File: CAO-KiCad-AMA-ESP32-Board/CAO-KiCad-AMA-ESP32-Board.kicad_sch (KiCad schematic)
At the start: 85 parts, among them J13 DHT Sensor, J14 Pot, J15 Select A, J16 Select B, J17 I2C, J3 Conn_01x19, J4 Conn_01x19, J5 Micro_SD_Card, J6 Servo, J7 I2C, J8 5V Ext, Q1 IRLML6402, SW1 SW_Push, SW2 SW_Push, SW3 SW_Push, SW4 SW_Push, SW5 SW_Push, SW6 SW_Push, U1 ESP32-DevKitC, U2 74HC595, Y1 Crystal_GND3_Small

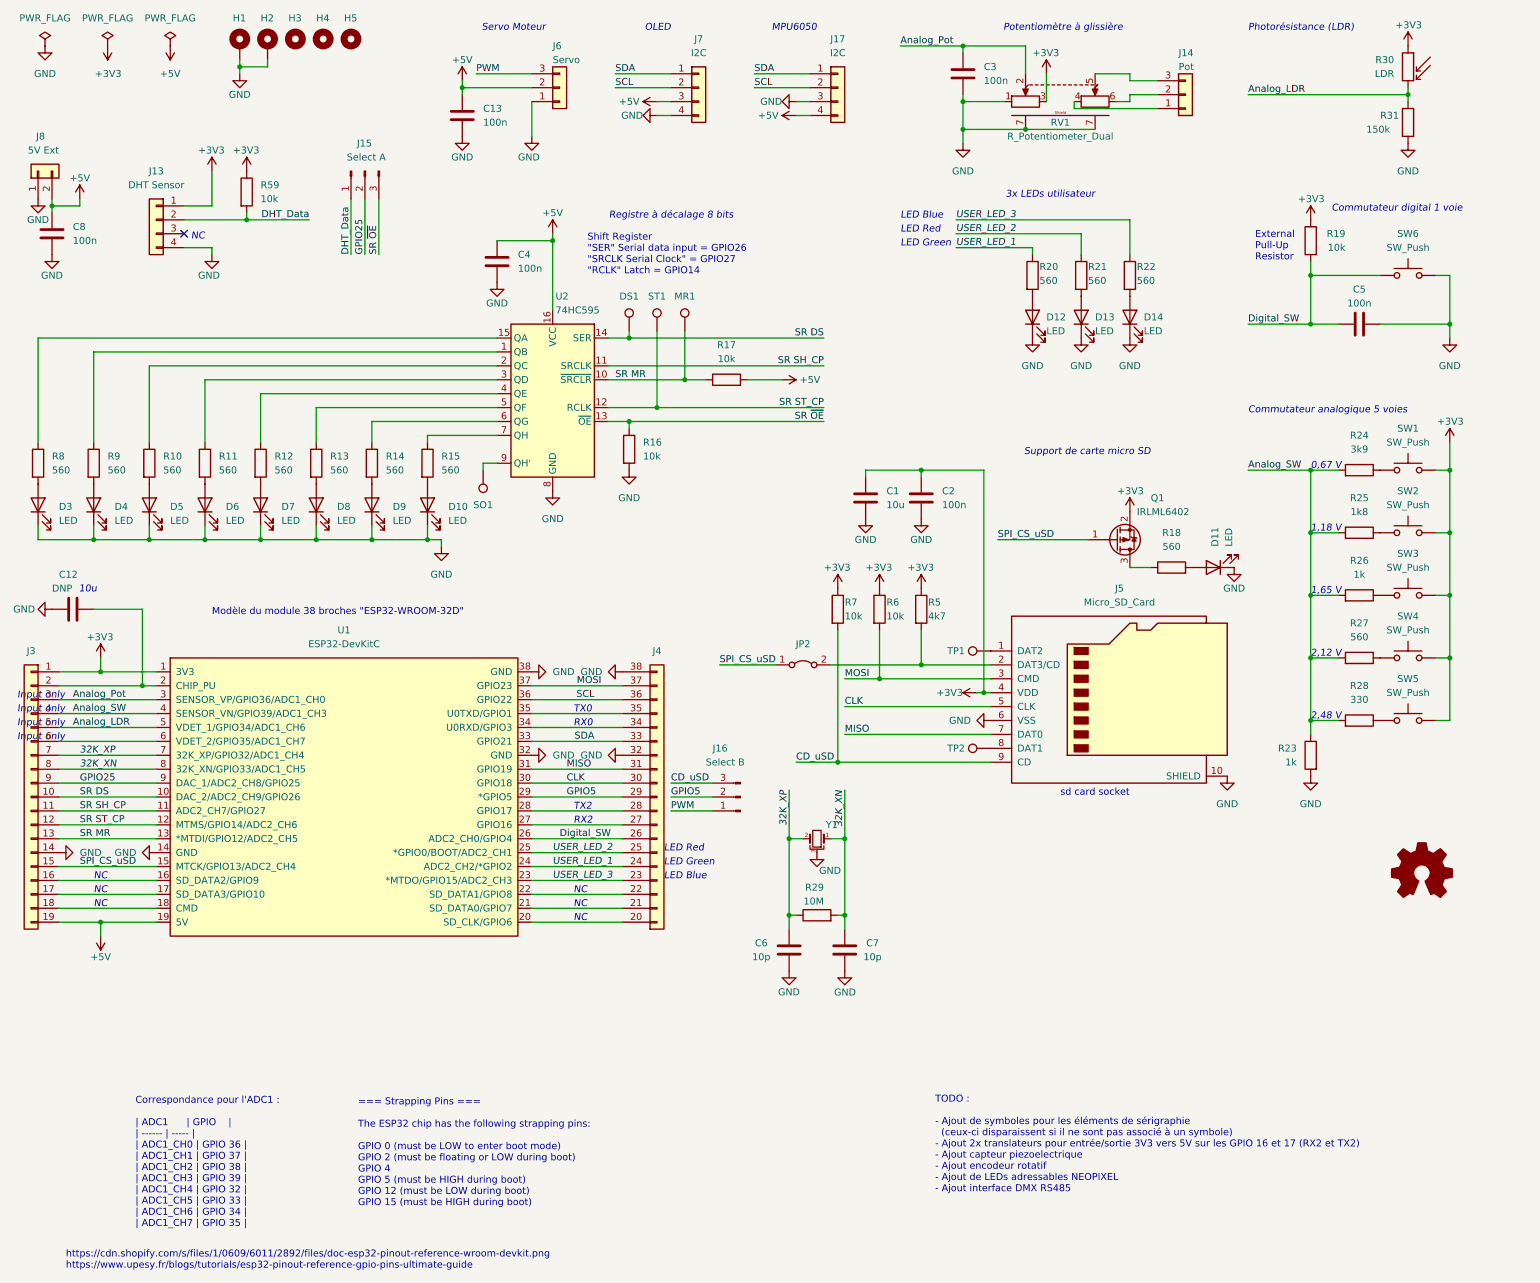
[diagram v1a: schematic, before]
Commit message: Correction majeur sur le GPIO12, doit-être à l'état bas lors du démarrage de l'ESP32
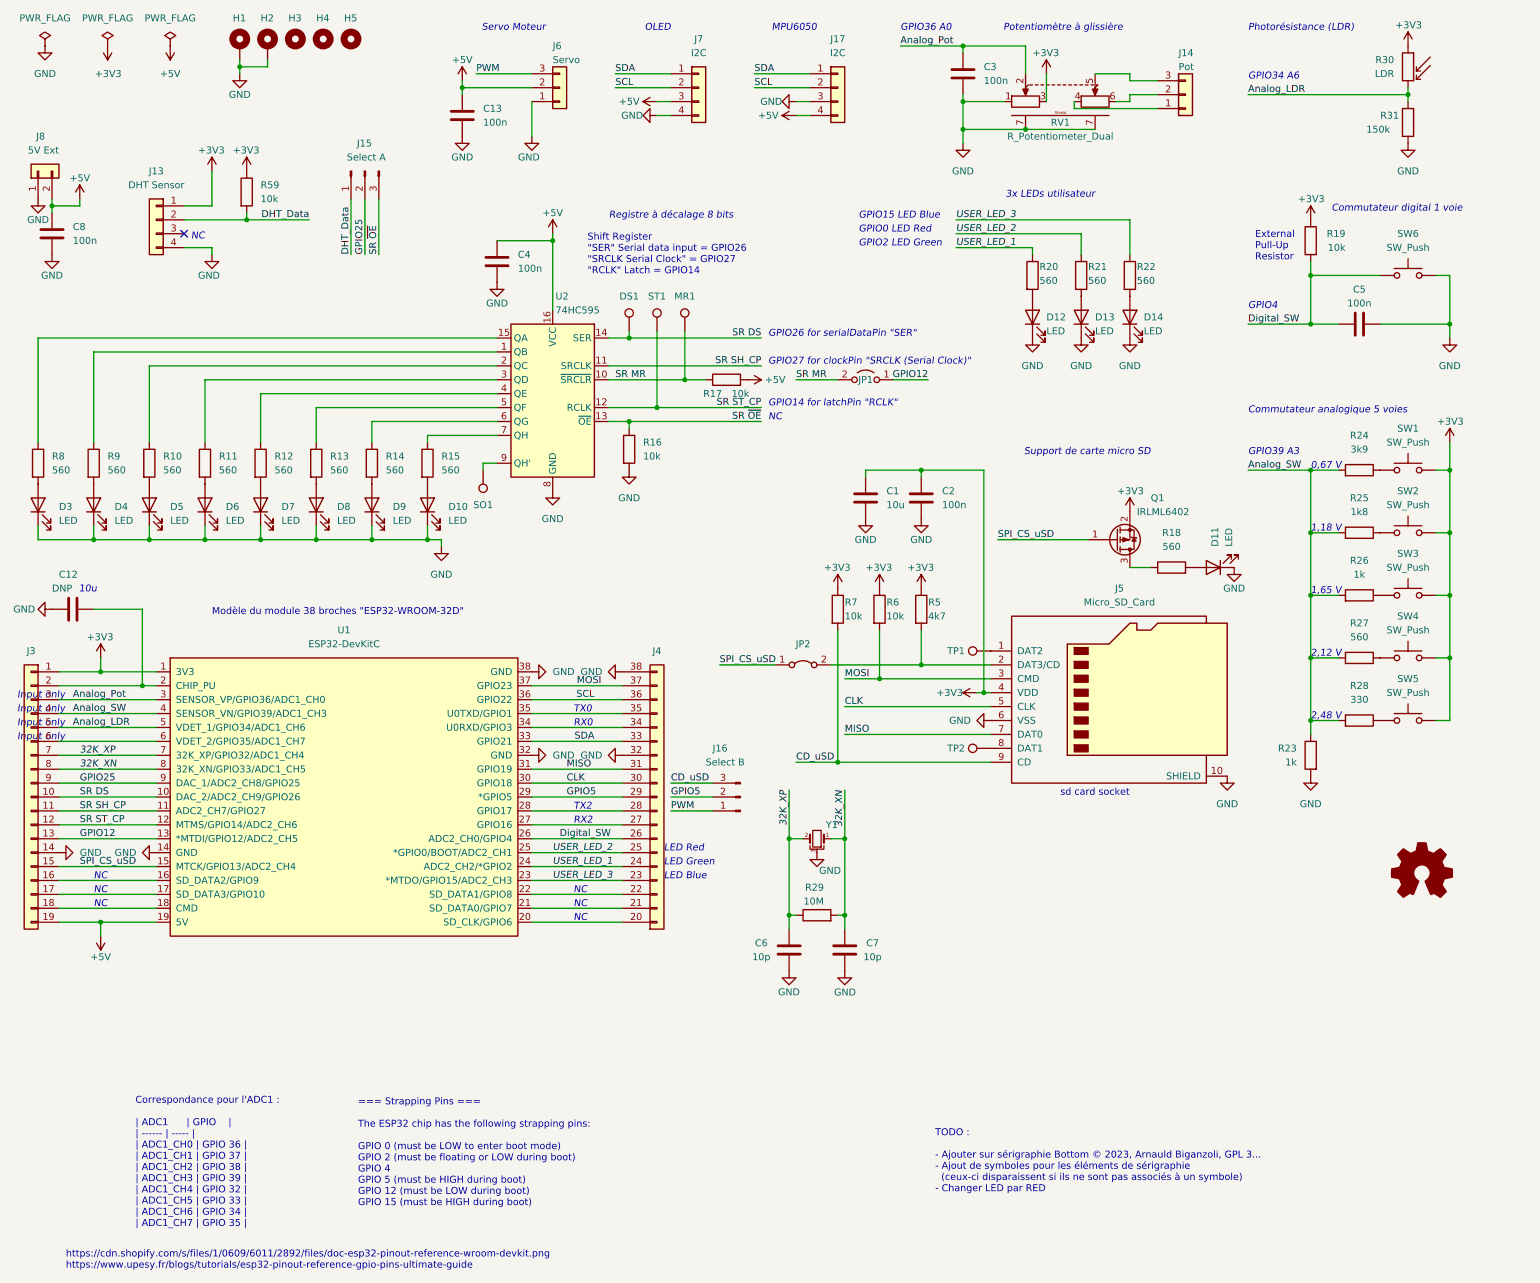
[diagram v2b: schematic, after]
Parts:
- added JP1: Jumper_2_Open, Jumper:SolderJumper-2_P1.3mm_Open_RoundedPad1.0x1.5mm, symbol Jumper:Jumper_2_Open
- Q1: Marking (none) -> EKWAB
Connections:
- net SR MR: now also JP1.2 (B); no longer J3.13 (Pin_13), U1.13 (*MTDI/GPIO12/ADC2_CH5)
- new net GPIO12: J3.13 (Pin_13), JP1.1 (A), U1.13 (*MTDI/GPIO12/ADC2_CH5)
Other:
- note added: "GPIO0 LED Red"
- note added: "GPIO14 for latchPin "RCLK""
- note added: "GPIO15 LED Blue"
- note added: "GPIO2 LED Green"
- note added: "GPIO26 for serialDataPin "SER""
- note added: "GPIO27 for clockPin "SRCLK (Serial Clock)""
- note added: "GPIO34 A6"
- note added: "GPIO36 A0"
- note added: "GPIO39 A3"
- note added: "GPIO4"
- note added: "TODO : - Ajouter sur sérigraphie Bottom © 2023, Arnauld Biganzoli, GPL 3... - Ajout de symboles pour les éléments de sérigraphie (ceux-ci disparaissent si ils ne sont pas associés à un symbole) - Changer LED par RED"
- note removed: "TODO : - Ajout de symboles pour les éléments de sérigraphie (ceux-ci disparaissent si il ne sont pas associé à un symbole) - Ajout 2x translateurs pour entrée/sortie 3V3 vers 5V sur les GPIO 16 et 17 (RX2 et TX2) - Ajout capteur piezoelectrique - Ajout encodeur rotatif - Ajout de LEDs adressables NEOPIXEL - Ajout interface DMX RS485"
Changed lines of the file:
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@@
     (stroke (width 0) (type default) (color 0 0 0 0))
   )
-  (wire (pts (xy 149.86 83.82) (xy 156.21 83.82))
-    (stroke (width 0) (type default) (color 0 0 0 0))
-  )
   (wire (pts (xy 252.73 73.66) (xy 241.3 73.66))
     (stroke (width 0) (type default) (color 0 0 0 0))
@@
     (stroke (width 0) (type default) (color 0 0 0 0))
   )
-  (wire (pts (xy 128.27 91.44) (xy 163.83 91.44))
+  (wire (pts (xy 128.27 91.44) (xy 152.4 91.44))
     (stroke (width 0) (type default) (color 0 0 0 0))
   )
@@
     (stroke (width 0) (type default) (color 0 0 0 0))
   )
+  (wire (pts (xy 158.75 83.82) (xy 166.37 83.82))
+    (stroke (width 0) (type default) (color 0 0 0 0))
+  )
   (wire (pts (xy 20.32 110.49) (xy 20.32 113.03))
     (stroke (width 0) (type default) (color 0 0 0 0))
@@
     (stroke (width 0) (type default) (color 0 0 0 0))
   )
-  (wire (pts (xy 128.27 76.2) (xy 163.83 76.2))
+  (wire (pts (xy 128.27 76.2) (xy 152.4 76.2))
     (stroke (width 0) (type default) (color 0 0 0 0))
   )
@@
     (stroke (width 0) (type default) (color 0 0 0 0))
   )
-  (wire (pts (xy 124.46 81.28) (xy 163.83 81.28))
+  (wire (pts (xy 124.46 81.28) (xy 152.4 81.28))
+    (stroke (width 0) (type default) (color 0 0 0 0))
+  )
+  (wire (pts (xy 182.88 83.82) (xy 176.53 83.82))
     (stroke (width 0) (type default) (color 0 0 0 0))
   )
@@
     (stroke (width 0) (type default) (color 0 0 0 0))
   )
-  (wire (pts (xy 133.35 88.9) (xy 163.83 88.9))
+  (wire (pts (xy 133.35 88.9) (xy 152.4 88.9))
     (stroke (width 0) (type default) (color 0 0 0 0))
   )
@@
     (effects (font (size 1.27 1.27) italic) (justify right bottom))
   )
-  (text "LED Red" (at 177.8 57.15 0)
+  (text "GPIO0 LED Red" (at 170.18 57.15 0)
     (effects (font (size 1.27 1.27) italic) (justify left bottom))
   )
@@
     (effects (font (size 1.27 1.27) italic) (justify left bottom))
   )
+  (text "GPIO39 A3" (at 241.3 97.79 0)
+    (effects (font (size 1.27 1.27) italic) (justify left bottom))
+  )
   (text "RX0" (at 118.11 147.32 0)
     (effects (font (size 1.27 1.27) italic) (justify left bottom))
@@
     (effects (font (size 1.27 1.27) italic) (justify right bottom))
   )
+  (text "NC" (at 153.67 91.44 0)
+    (effects (font (size 1.27 1.27) italic) (justify left bottom))
+  )
   (text "NC" (at 118.11 180.34 0)
     (effects (font (size 1.27 1.27) italic) (justify left bottom))
@@
     (effects (font (size 1.27 1.27) italic) (justify left bottom))
   )
+  (text "GPIO14 for latchPin \"RCLK\"" (at 153.67 88.9 0)
+    (effects (font (size 1.27 1.27) italic) (justify left bottom))
+  )
   (text "NC" (at 30.48 175.26 0)
     (effects (font (size 1.27 1.27) italic) (justify left bottom))
@@
     (effects (font (size 1.27 1.27) italic) (justify left bottom))
   )
-  (text "LED Blue" (at 177.8 54.61 0)
+  (text "GPIO4" (at 241.3 71.12 0)
+    (effects (font (size 1.27 1.27) italic) (justify left bottom))
+  )
+  (text "GPIO15 LED Blue" (at 170.18 54.61 0)
     (effects (font (size 1.27 1.27) italic) (justify left bottom))
   )
-  (text "TODO :\n\n- Ajout de symboles pour les éléments de sérigraphie\n  (ceux-ci disparaissent si il ne sont pas associé à un symbole)\n- Ajout 2x translateurs pour entrée/sortie 3V3 vers 5V sur les GPIO 16 et 17 (RX2 et TX2)\n- Ajout capteur piezoelectrique\n- Ajout encodeur rotatif\n- Ajout de LEDs adressables NEOPIXEL\n- Ajout interface DMX RS485"
+  (text "TODO :\n\n- Ajouter sur sérigraphie Bottom © 2023, Arnauld Biganzoli, GPL 3...\n- Ajout de symboles pour les éléments de sérigraphie\n  (ceux-ci disparaissent si ils ne sont pas associés à un symbole)\n- Changer LED par RED"
     (at 184.15 232.41 0)
     (effects (font (size 1.27 1.27)) (justify left bottom))
@@
     (effects (font (size 1.27 1.27) italic) (justify left bottom))
   )
-  (text "LED Green" (at 177.8 59.69 0)
+  (text "GPIO26 for serialDataPin \"SER\"" (at 153.67 76.2 0)
+    (effects (font (size 1.27 1.27) italic) (justify left bottom))
+  )
+  (text "GPIO2 LED Green" (at 170.18 59.69 0)
     (effects (font (size 1.27 1.27) italic) (justify left bottom))
   )
@@
     (effects (font (size 1.27 1.27)) (justify left bottom))
   )
+  (text "GPIO27 for clockPin \"SRCLK (Serial Clock)\"" (at 153.67 81.28 0)
+    (effects (font (size 1.27 1.27) italic) (justify left bottom))
+  )
   (text "NC" (at 48.26 58.42 0)
     (effects (font (size 1.27 1.27) italic) (justify left bottom))
@@
     (effects (font (size 1.27 1.27) italic) (justify right bottom))
   )
+  (text "GPIO34 A6" (at 241.3 29.21 0)
+    (effects (font (size 1.27 1.27) italic) (justify left bottom))
+  )
   (text "NC" (at 30.48 177.8 0)
     (effects (font (size 1.27 1.27) italic) (justify left bottom))
@@
     (effects (font (size 1.27 1.27) italic) (justify left bottom))
   )
+  (text "GPIO36 A0" (at 177.8 20.32 0)
+    (effects (font (size 1.27 1.27) italic) (justify left bottom))
+  )
   (text "Input only" (at 16.51 142.24 0)
     (effects (font (size 1.27 1.27) italic) (justify left bottom))
@@
     (effects (font (size 1.27 1.27) italic) (justify right bottom))
   )
-  (label "SR ST_CP" (at 163.83 88.9 180)
+  (label "SR ST_CP" (at 152.4 88.9 180)
     (effects (font (size 1.27 1.27)) (justify right bottom))
   )
@@
     (effects (font (size 1.27 1.27)) (justify left bottom))
   )
-  (label "SR DS" (at 163.83 76.2 180)
+  (label "SR DS" (at 152.4 76.2 180)
     (effects (font (size 1.27 1.27)) (justify right bottom))
   )
@@
     (effects (font (size 1.27 1.27)) (justify left bottom))
   )
-  (label "SR MR" (at 27.94 167.64 0)
+  (label "SR MR" (at 158.75 83.82 0)
     (effects (font (size 1.27 1.27)) (justify left bottom))
   )
@@
     (effects (font (size 1.27 1.27)) (justify left bottom))
   )
-  (label "SR ~{OE}" (at 163.83 91.44 180)
+  (label "SR ~{OE}" (at 152.4 91.44 180)
+    (effects (font (size 1.27 1.27)) (justify right bottom))
+  )
+  (label "GPIO12" (at 182.88 83.82 180)
     (effects (font (size 1.27 1.27)) (justify right bottom))
   )
@@
     (effects (font (size 1.27 1.27)) (justify left bottom))
   )
-  (label "SR SH_CP" (at 163.83 81.28 180)
+  (label "SR SH_CP" (at 152.4 81.28 180)
     (effects (font (size 1.27 1.27)) (justify right bottom))
   )
@@
     (effects (font (size 1.27 1.27) italic) (justify right bottom))
   )
+  (label "GPIO12" (at 27.94 167.64 0)
+    (effects (font (size 1.27 1.27)) (justify left bottom))
+  )
   (symbol (lib_id "power:GND") (at 270.51 40.64 0) (unit 1)
     (in_bom yes) (on_board yes) (fields_autoplaced)
@@
     (pin "1")
   )
-  (symbol (lib_id "power:+5V") (at 156.21 83.82 270) (mirror x) (unit 1)
+  (symbol (lib_id "power:+5V") (at 149.86 83.82 270) (mirror x) (unit 1)
     (in_bom yes) (on_board yes)
-    (property "Reference" "#PWR0117" (id 0) (at 152.4 83.82 0)
+    (property "Reference" "#PWR0117" (id 0) (at 146.05 83.82 0)
       (effects (font (size 1.27 1.27)) hide)
     )
-    (property "Value" "+5V" (id 1) (at 161.29 83.82 90))
-    (property "Footprint" "" (id 2) (at 156.21 83.82 0)
+    (property "Value" "+5V" (id 1) (at 154.94 83.82 90))
+    (property "Footprint" "" (id 2) (at 149.86 83.82 0)
       (effects (font (size 1.27 1.27)) hide)
     )
-    (property "Datasheet" "" (id 3) (at 156.21 83.82 0)
+    (property "Datasheet" "" (id 3) (at 149.86 83.82 0)
       (effects (font (size 1.27 1.27)) hide)
     )
@@
     (pin "2")
   )
+  (symbol (lib_id "Jumper:Jumper_2_Open") (at 171.45 83.82 0) (mirror y) (unit 1)
+    (in_bom yes) (on_board yes)
+    (property "Reference" "JP1" (id 0) (at 171.45 83.82 0))
+    (property "Value" "Jumper_2_Open" (id 1) (at 171.45 80.01 0)
+      (effects (font (size 1.27 1.27)) hide)
+    )
+    (property "Footprint" "Jumper:SolderJumper-2_P1.3mm_Open_RoundedPad1.0x1.5mm" (id 2) (at 171.45 83.82 0)
+      (effects (font (size 1.27 1.27)) hide)
+    )
+    (property "Datasheet" "~" (id 3) (at 171.45 83.82 0)
+      (effects (font (size 1.27 1.27)) hide)
+    )
+    (pin "1")
+    (pin "2")
+  )
   (symbol (lib_id "Connector_Generic:Conn_01x03") (at 115.57 30.48 0) (mirror x) (unit 1)
     (in_bom yes) (on_board yes)
@@
       (effects (font (size 1.27 1.27)) (justify left) hide)
     )
+    (property "Marking" "EKWAB" (id 4) (at 217.17 113.03 0)
+      (effects (font (size 1.27 1.27)) hide)
+    )
     (pin "1")
     (pin "2")
@@
   )
   (symbol (lib_id "Device:R") (at 146.05 83.82 90) (unit 1)
-    (in_bom yes) (on_board yes) (fields_autoplaced)
-    (property "Reference" "R17" (id 0) (at 146.05 77.47 90))
-    (property "Value" "10k" (id 1) (at 146.05 80.01 90))
+    (in_bom yes) (on_board yes)
+    (property "Reference" "R17" (id 0) (at 143.51 86.36 90))
+    (property "Value" "10k" (id 1) (at 148.59 86.36 90))
     (property "Footprint" "Resistor_SMD:R_0805_2012Metric_Pad1.20x1.40mm_HandSolder" (id 2) (at 146.05 85.598 90)
       (effects (font (size 1.27 1.27)) hide)
@@
       (reference "J17") (unit 1) (value "I2C") (footprint "Connector_PinSocket_2.54mm:PinSocket_1x04_P2.54mm_Vertical")
     )
+    (path "/48a52053-1163-43d0-a4f3-8764e8fe8b0a"
+      (reference "JP1") (unit 1) (value "Jumper_2_Open") (footprint "Jumper:SolderJumper-2_P1.3mm_Open_RoundedPad1.0x1.5mm")
+    )
     (path "/a380c107-ff45-4f49-b4ff-7b86f6c70376"
